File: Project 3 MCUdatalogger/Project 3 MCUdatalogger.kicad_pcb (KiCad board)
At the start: 2 copper layers, 29 parts, among them J1 Conn_01x04_Pin, J2 Conn_01x09_Pin, J3 Conn_01x04_Pin, J4 Conn_02x03_Odd_Even, U1 24LC1025, U2 DS1337S_, U3 24LC1025, U4 ATMEGA328P-AU, Y1 32.768 KHz, Y2 16 MHz

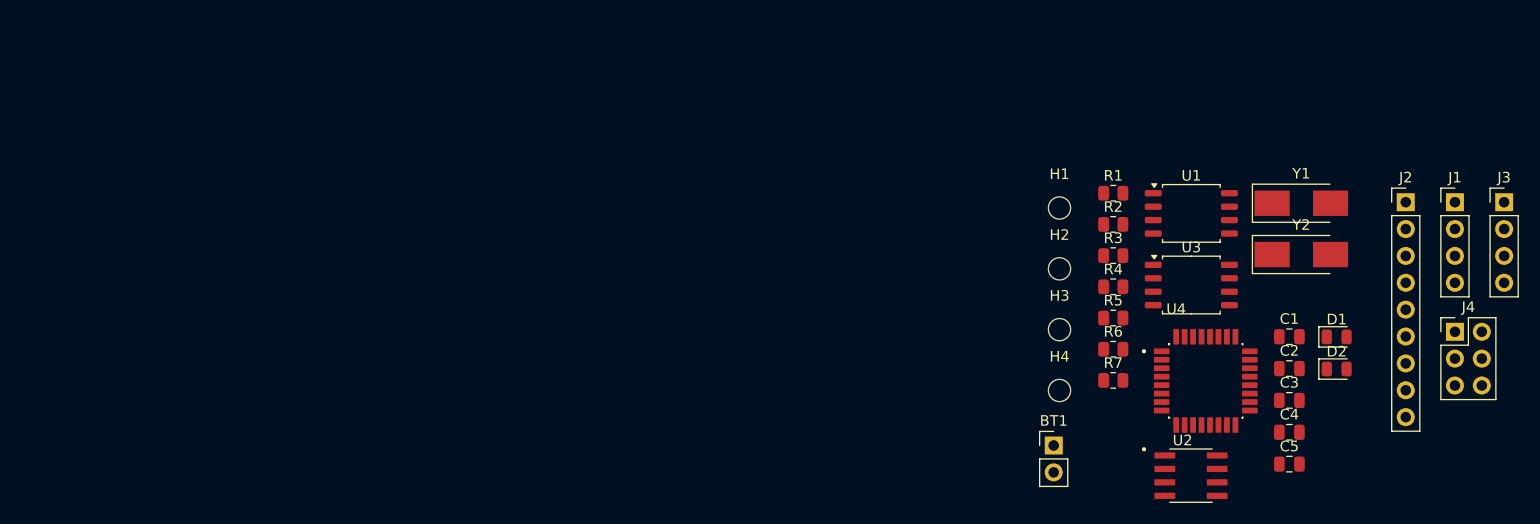
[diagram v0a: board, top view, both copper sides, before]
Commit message: Complete Placement of Footprints.
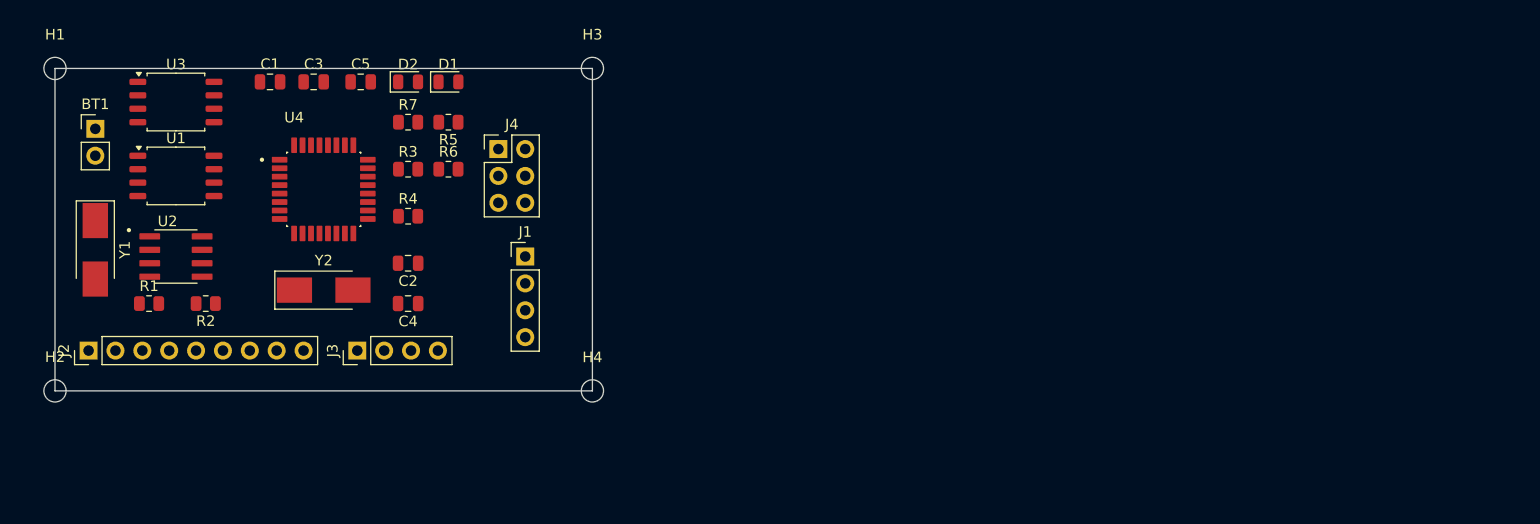
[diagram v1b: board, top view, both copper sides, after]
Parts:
- moved J2 125.3 mm to (41.3, 85.1), turned to 90 degrees
- moved Y1 114.1 mm to (41.9, 75.6), turned to -90 degrees
- moved J3 109.3 mm to (66.7, 85.1), turned to 90 degrees
- moved C1 99.3 mm to (58.4, 59.7)
- moved U2 98.2 mm to (49.5, 76.2)
- moved U3 97.5 mm to (49.5, 61.6)
- moved C3 97.0 mm to (62.5, 59.7)
- moved U1 96.0 mm to (49.5, 68.6)
- moved H1 95.9 mm to (38.1, 58.4)
- moved H2 95.7 mm to (38.1, 88.9)
- moved BT1 95.4 mm to (41.9, 64.1)
- moved C5 94.9 mm to (67.0, 59.7)
- moved Y2 92.5 mm to (63.5, 79.4)
- moved J4 92.1 mm to (80.0, 66.0)
- moved D2 91.9 mm to (71.5, 59.7)
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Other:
- board outline added: 50.8 x 30.5 mm

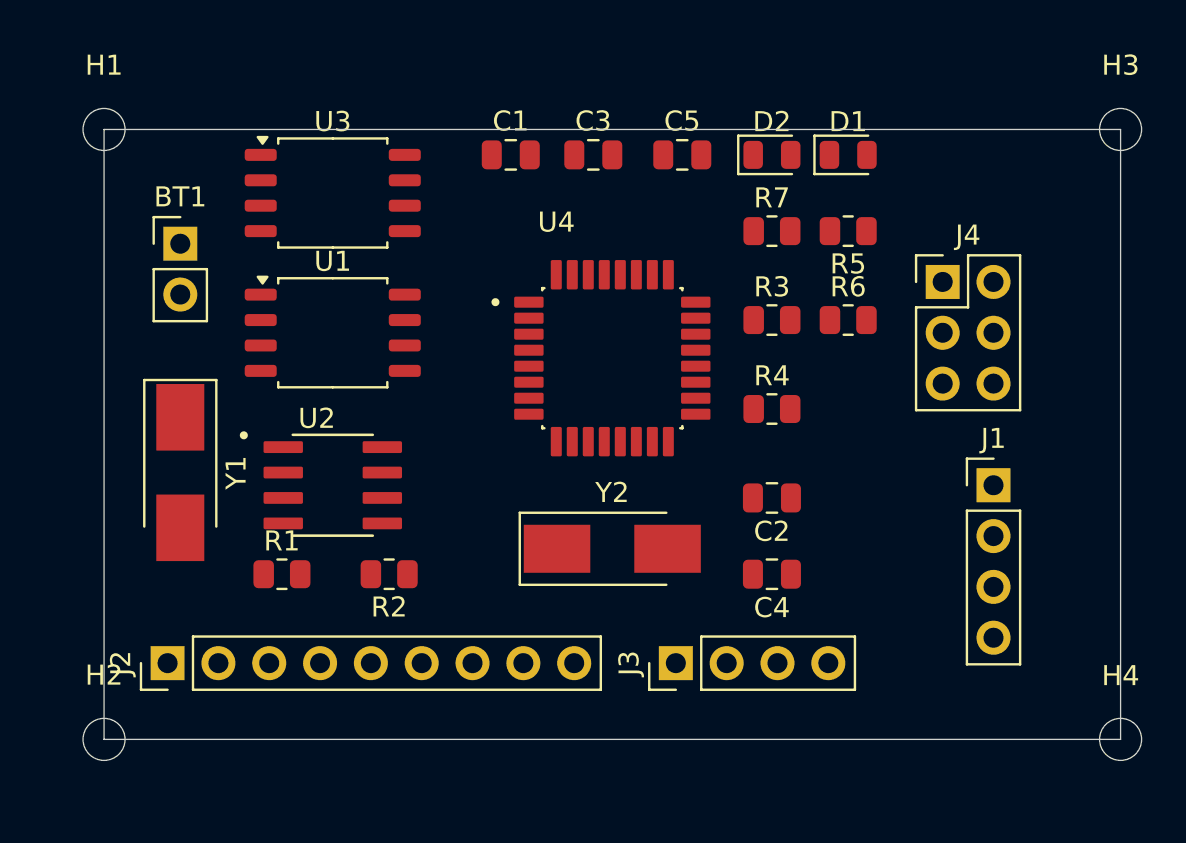
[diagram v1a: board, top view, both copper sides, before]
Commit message: Routing sans GND Vcc complete.
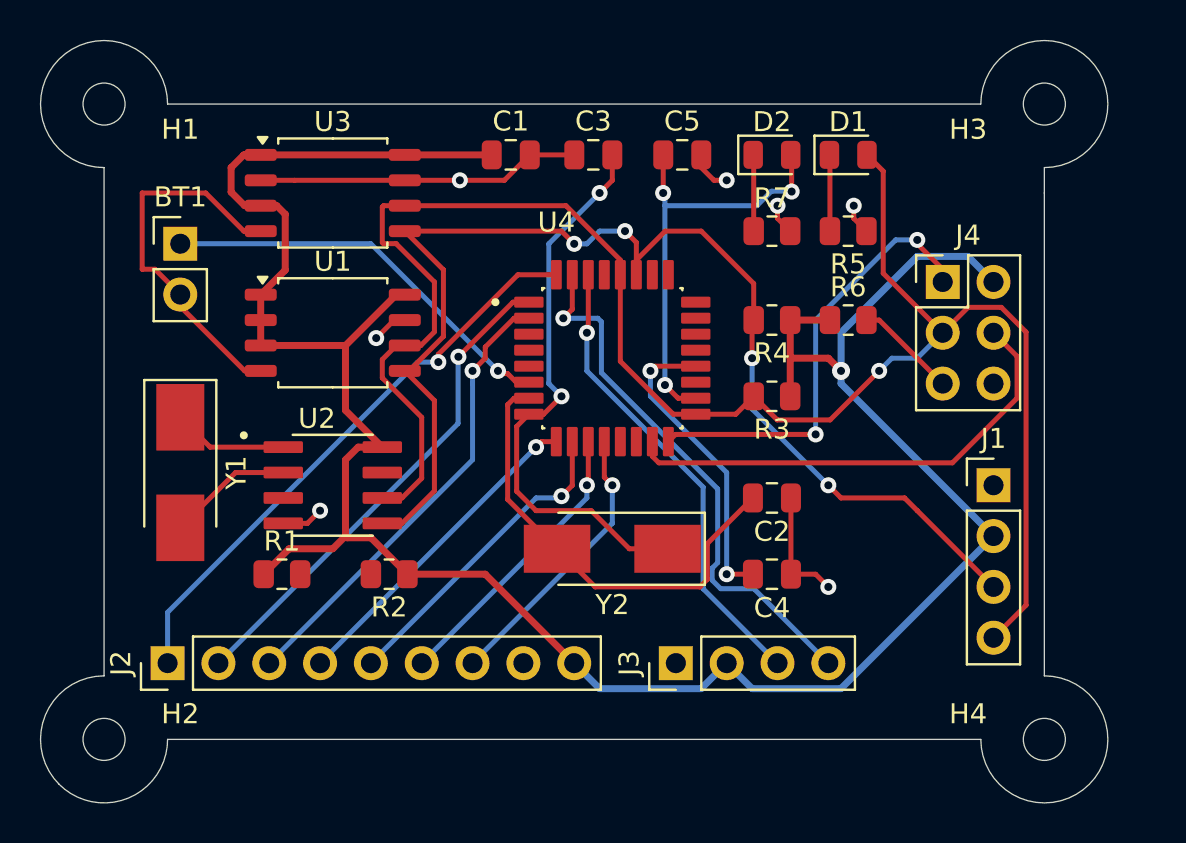
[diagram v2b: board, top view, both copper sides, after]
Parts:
- moved R4 4.45 mm to (71.5, 67.9), turned to 180 degrees
- moved H3 4.02 mm to (85.1, 57.1)
- moved H4 3.81 mm to (85.1, 88.9)
- moved R3 3.81 mm to (71.5, 71.8), turned to 180 degrees
- moved H1 1.27 mm to (38.1, 57.1)
- turned Y2 to 180 degrees
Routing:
- net /Vcc: track 0.00 -> 121.0 mm, vias 0 -> 1
- net /SCK: track 0.00 -> 89.6 mm, vias 0 -> 1
- net /SDA: track 0.00 -> 62.9 mm, vias 0 -> 4
- net GND: track 0.00 -> 50.4 mm, vias 0 -> 7
- net Net-(BT1-+): track 0.00 -> 42.2 mm, vias 0 -> 4
- net /D2: track 0.00 -> 29.2 mm, vias 0 -> 1
- net Net-(U4-PB7): track 0.00 -> 28.5 mm, vias 0 -> 2
- net /TX: track 0.00 -> 27.4 mm, vias 0 -> 1
- net /D3: track 0.00 -> 24.9 mm, vias 0 -> 1
- net /MOSI: track 0.00 -> 24.2 mm
- net /RX: track 0.00 -> 23.4 mm, vias 0 -> 1
- net /D4: track 0.00 -> 23.0 mm, vias 0 -> 1
- net Net-(U4-PB6): track 0.00 -> 22.9 mm
- net /MISO: track 0.00 -> 22.6 mm, vias 0 -> 2
- net /D5: track 0.00 -> 16.4 mm, vias 0 -> 1
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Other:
- board size 50.8 x 30.5 mm -> 53.3 x 38.1 mm

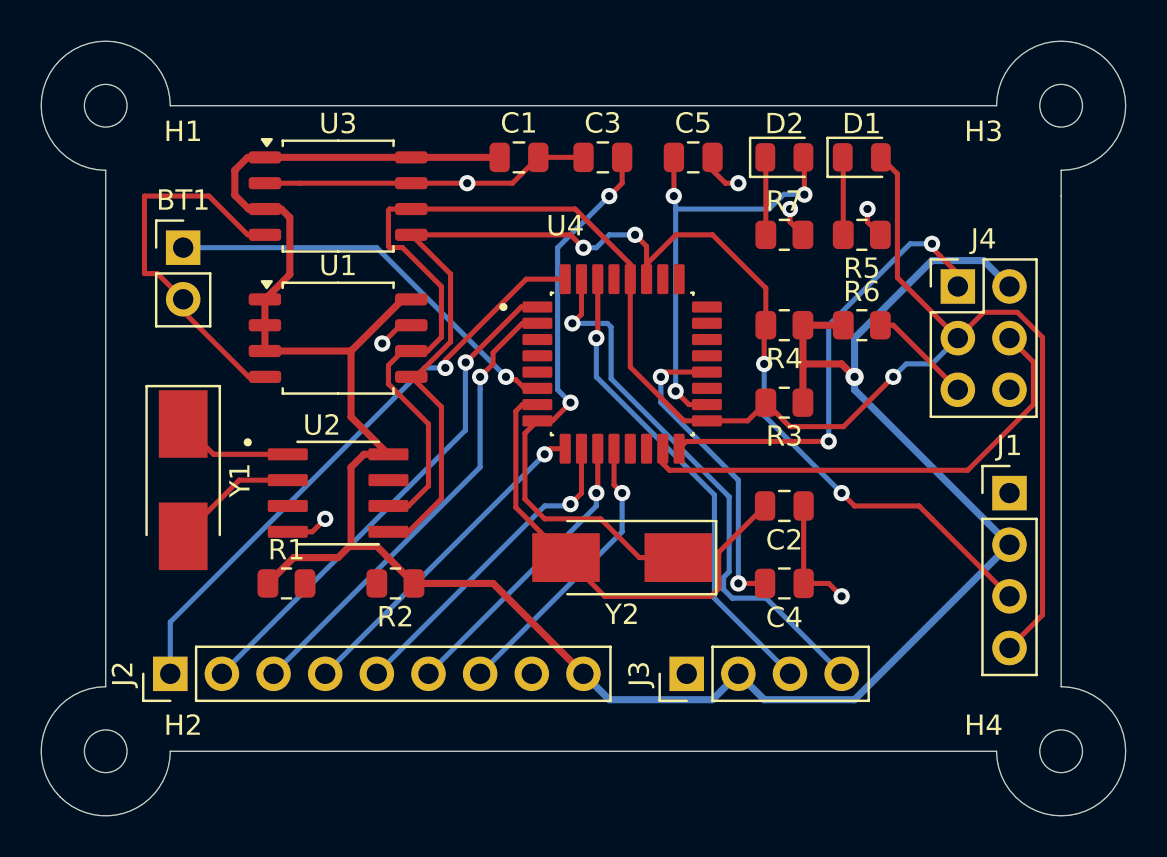
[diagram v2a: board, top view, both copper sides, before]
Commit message: Completed routing
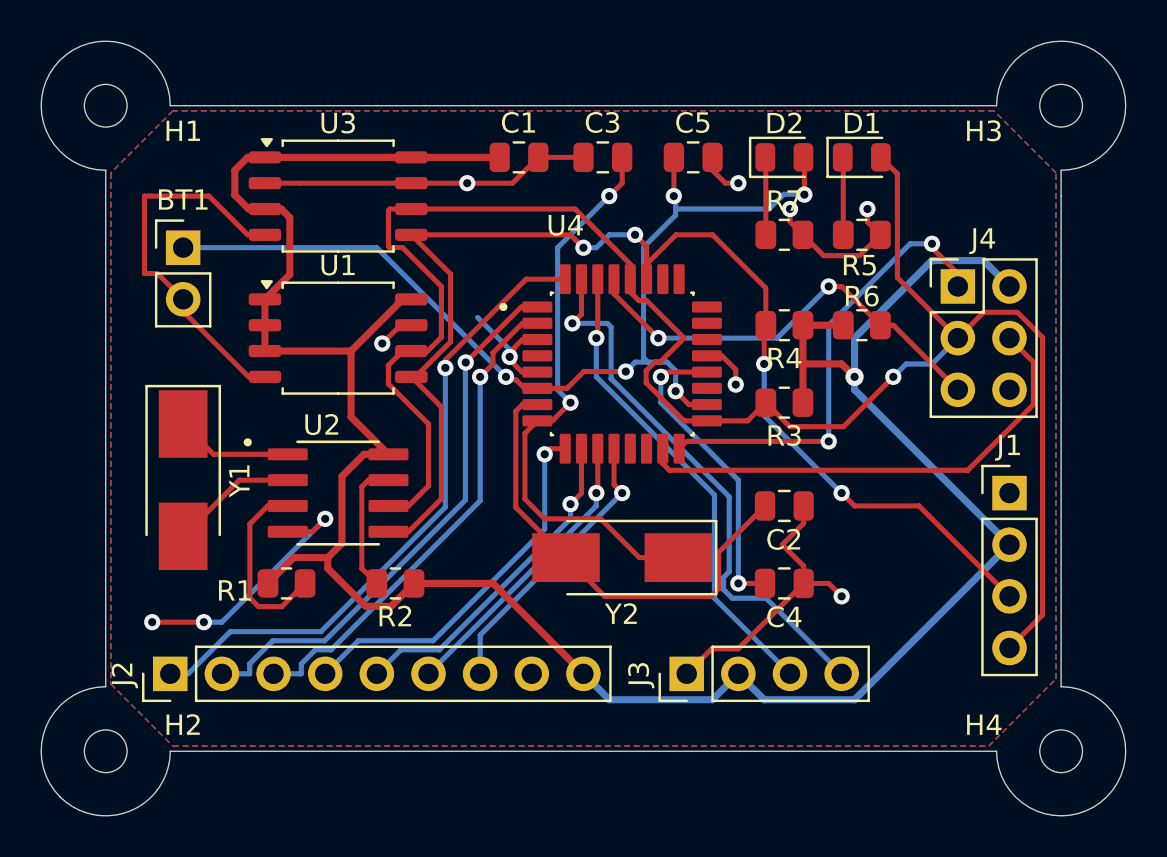
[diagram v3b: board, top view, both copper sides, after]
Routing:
- net GND: track 50.4 -> 82.8 mm, vias 7 -> 11
- net /RESET: track 5.13 -> 21.7 mm, vias 0 -> 2
- net Net-(U2-~{INTA}): track 0.00 -> 9.24 mm
- net Net-(BT1-+): track 42.2 -> 50.0 mm, vias 4 -> 5
- net Net-(U2-SQW/~INT): track 0.00 -> 6.51 mm
- net /D2: track 29.2 -> 31.7 mm
- net /D3: track 24.9 -> 27.2 mm
- net /D5: track 16.4 -> 18.5 mm
- net /SCK: track 89.6 -> 91.5 mm
- net /Vcc: track 121.0 -> 122.9 mm
- net /D4: track 23.0 -> 24.3 mm
- added copper zone on F.Cu, net /Vcc
- added copper zone on B.Cu, net GND

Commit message: Refined Routing Complete
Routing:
- net GND: track 82.8 -> 68.7 mm, vias 11 -> 12

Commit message: Fixed outstanding issues
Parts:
- moved BT1 1.78 mm to (40.1, 64.1)
- moved Y1 1.53 mm to (40.4, 75.4)
- moved J3 1.27 mm to (67.7, 85.9)
- moved H1 1.27 mm to (38.1, 58.4)
- moved H3 1.27 mm to (85.1, 58.4)
- moved J2 1.27 mm to (42.3, 85.9)
- moved H2 0.89 mm to (38.1, 88.0)
- moved H4 0.89 mm to (85.1, 88.0)
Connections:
- BT1 pad 1: Net-(BT1-+) -> /Vcc
- C5 pad 1: Net-(BT1-+) -> /Vcc
- D2 pad 2: Net-(BT1-+) -> /Vcc
- U4 pad 18: Net-(BT1-+) -> /Vcc
- U4 pad 6: Net-(BT1-+) -> /Vcc
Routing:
- net Net-(BT1-+): track 50.0 -> 0.00 mm, vias 5 -> 0
- net GND: track 68.7 -> 52.4 mm, vias 12 -> 10
- net /Vcc: track 122.9 -> 131.4 mm, vias 1 -> 6
- net /SCK: track 91.5 -> 94.2 mm
- net /MOSI: track 24.2 -> 22.4 mm
- net /RX: track 23.4 -> 25.0 mm
- net Net-(U2-X1): track 5.76 -> 7.34 mm
- net Net-(U2-X2): track 6.58 -> 8.05 mm
- net /TX: track 27.3 -> 28.7 mm
- net /D6: track 16.4 -> 15.7 mm
- net /D5: track 18.5 -> 17.9 mm
- net Net-(U4-AREF): track 15.4 -> 14.8 mm
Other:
- board size 53.3 x 38.1 mm -> 53.1 x 35.7 mm
- board text added: "2"
- board text added: "3"
- board text added: "4"
- board text added: "5"
- board text added: "6"
- board text added: "7"
- board text added: "8"
- board text added: "GND"
- board text added: "GPIO"
- board text added: "I2C"
- board text added: "ICSP"
- board text added: "ICSP MISO |VCC SCK |MOSI RESET|GND"
- board text added: "RX"
- board text added: "SCK"
- board text added: "SDA"
- board text added: "SERIAL"
- board text added: "TX"
- board text added: "Vcc"

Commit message: Added Finishing touches and Gerber Files
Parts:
- added REF**: KiCad-Logo2_6mm_SilkScreen, Symbol:KiCad-Logo2_6mm_SilkScreen, B.Cu at (62.1, 76.2)
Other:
- board text added: "- 2Mbit EEPROM - RTC - I2C, SPI, GPIOs"
- board text added: "0.2000 mm / 0.0000 mm"
- board text added: "0.3000 mm"
- board text added: "1.6000 mm"
- board text added: "53.0900 mm x 35.6910 mm"
- board text added: "BOARD CHARACTERISTICS"
- board text added: "Board Thickness:"
- board text added: "Board overall dimensions:"
- board text added: "Castellated pads:"
- board text added: "Copper Finish:"
- board text added: "Copper Layer Count:"
- board text added: "Data Logger with the ATMega328P."
- board text added: "Edge card connectors:"
- board text added: "Impedance Control:"
- board text added: "Min hole diameter:"
- board text added: "Min track/spacing:"
- board text added: "No"
- board text added: "None"
- board text added: "Plated Board Edge:"

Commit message: Routing
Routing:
- net /Vcc: track 131.4 -> 38.0 mm, vias 6 -> 12
- net GND: track 52.4 -> 35.7 mm, vias 10 -> 11
- net /D8: track 14.5 -> 23.2 mm, vias 1 -> 0
- net /SCK: track 94.2 -> 86.5 mm, vias 1 -> 5
- net /MISO: track 22.6 -> 27.8 mm
- net /RESET: track 22.0 -> 26.7 mm, vias 2 -> 1
- net /RX: track 25.0 -> 29.2 mm, vias 1 -> 0
- net Net-(U2-~{INTA}): track 9.24 -> 5.10 mm
- net Net-(U4-AREF): track 14.8 -> 18.8 mm
- net /TX: track 28.7 -> 32.4 mm, vias 1 -> 0
- net /D4: track 23.8 -> 26.7 mm, vias 1 -> 0
- net /MOSI: track 22.4 -> 25.0 mm, vias 0 -> 2
- net Net-(U4-PB6): track 23.4 -> 25.6 mm, vias 0 -> 3
- net Net-(U4-PB7): track 28.5 -> 26.3 mm, vias 2 -> 3
- net /D3: track 26.8 -> 28.7 mm, vias 1 -> 0
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- added copper zone on In2.Cu, net /Vcc
- removed copper zone on F.Cu, net /Vcc
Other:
- copper layers 2 -> 4
